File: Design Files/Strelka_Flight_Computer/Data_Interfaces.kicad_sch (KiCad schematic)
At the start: 10 parts

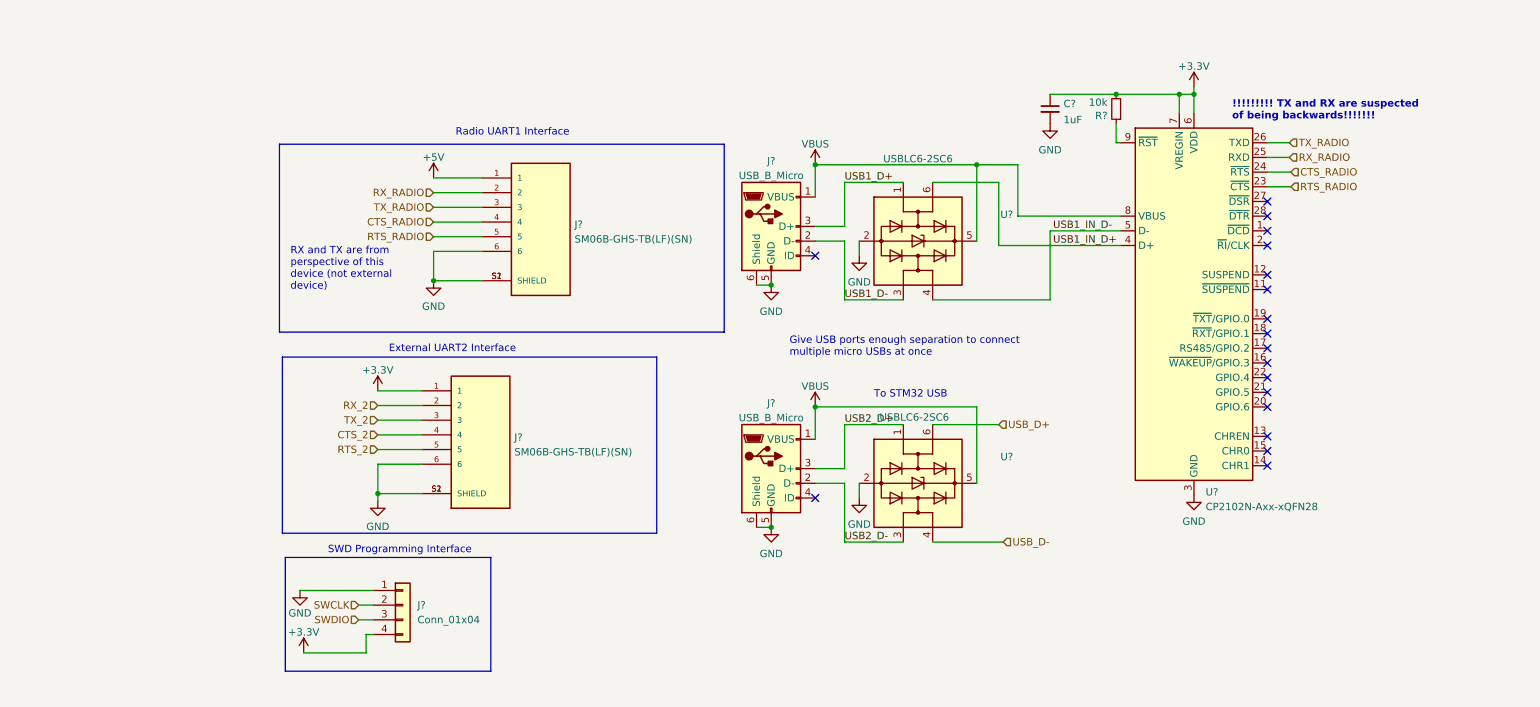
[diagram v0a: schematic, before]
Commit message: Added sensors
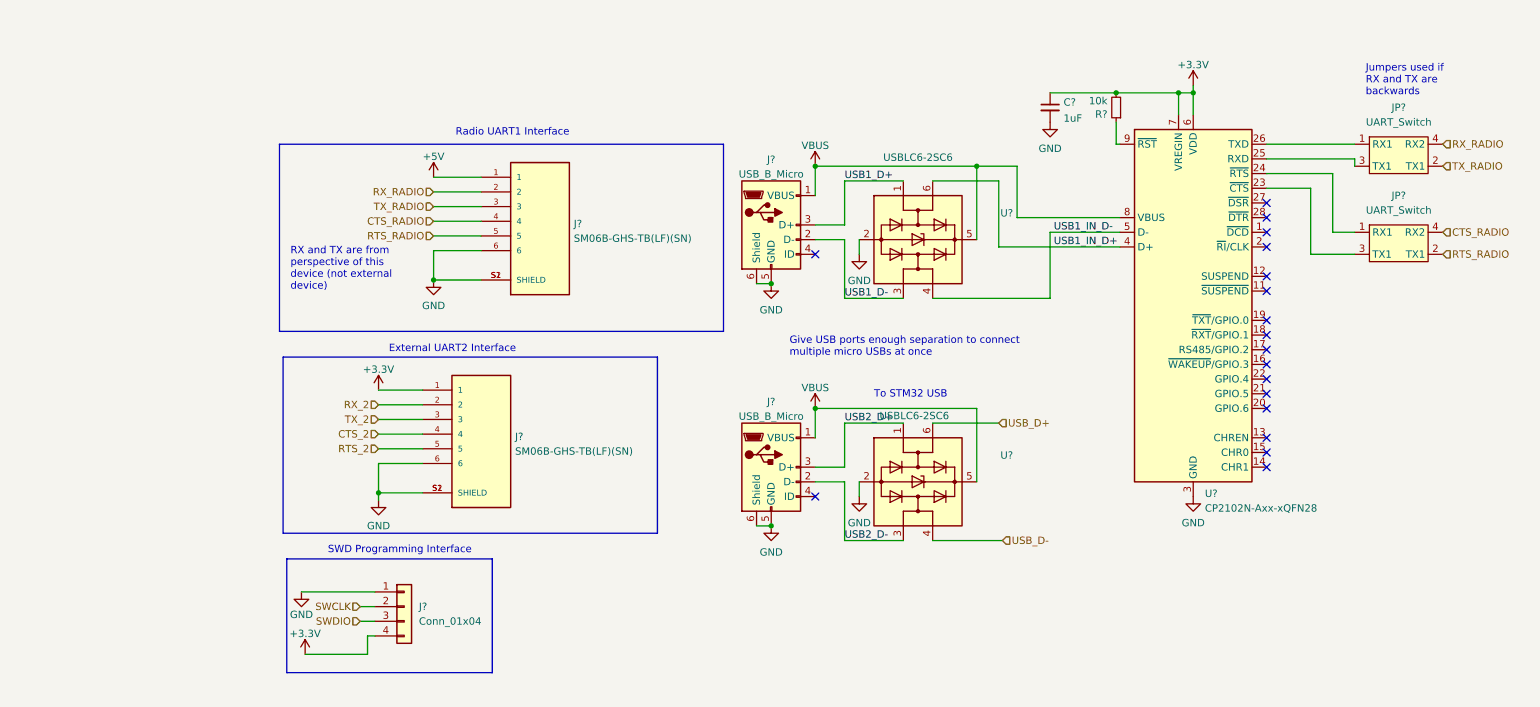
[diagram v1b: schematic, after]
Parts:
- added JP? (x2): UART_Switch, Footprints:UART_Switch, symbol UART_Switch:UART_Switch
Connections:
- net CTS_RADIO: now also JP?.4 (RX2); no longer U?.24 (~{RTS})
- net RTS_RADIO: now also JP?.2 (TX1); no longer U?.23 (~{CTS})
- net RX_RADIO: now also JP?.4 (RX2); no longer U?.25 (RXD)
- net TX_RADIO: now also JP?.2 (TX1); no longer U?.26 (TXD)
- new net: JP?.1 (RX1), U?.24 (~{RTS})
- new net: JP?.3 (TX1), U?.23 (~{CTS})
- new net: JP?.1 (RX1), U?.26 (TXD)
- new net: JP?.3 (TX1), U?.25 (RXD)
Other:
- note added: "Jumpers used if RX and TX are backwards"
- note removed: "!!!!!!!!! TX and RX are suspected of being backwards!!!!!!!"

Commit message: Working SPICE sim for ematch continuity circuit
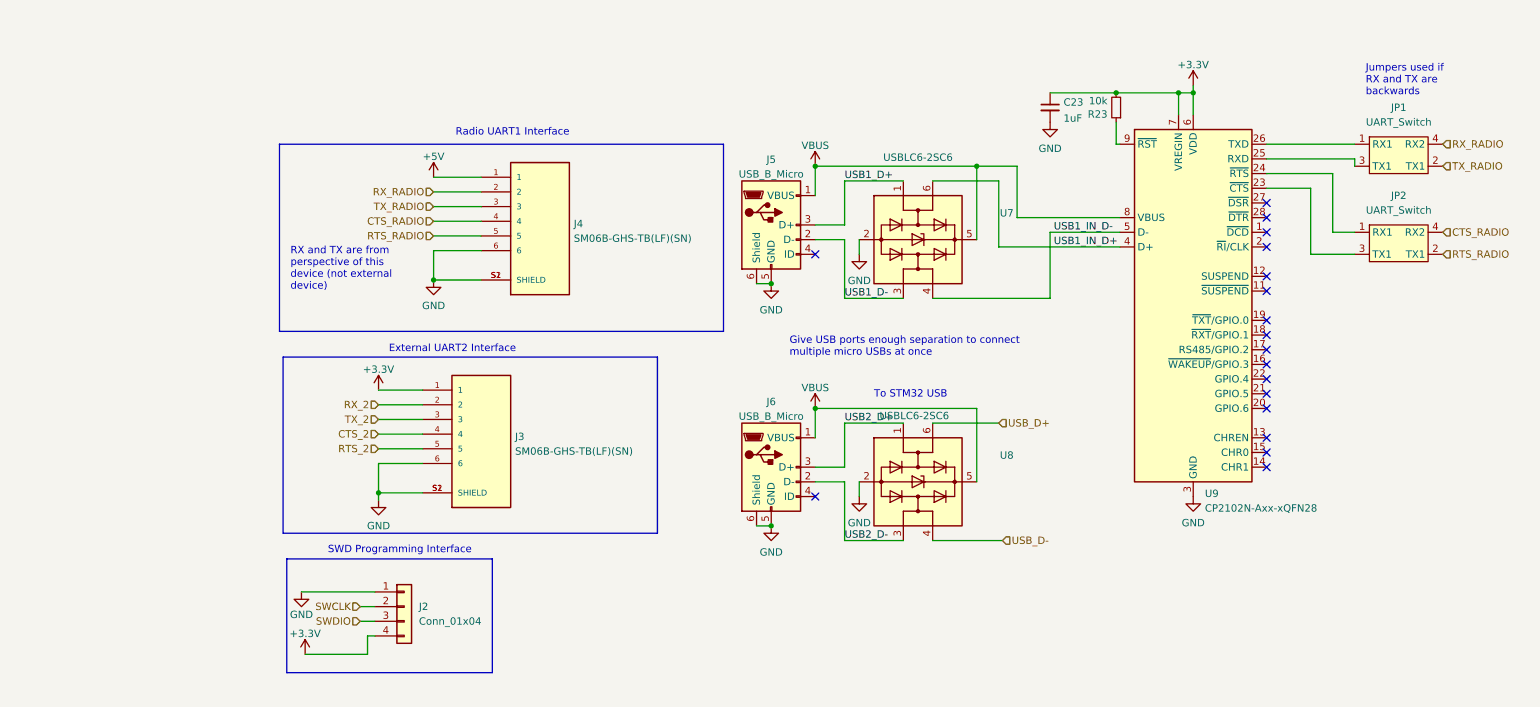
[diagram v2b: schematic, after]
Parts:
- gave numbers to parts that had none: 12
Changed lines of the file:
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@@
   (symbol (lib_id "power:GND") (at 84.455 100.965 0) (unit 1)
     (in_bom yes) (on_board yes) (fields_autoplaced)
-    (property "Reference" "#PWR?" (id 0) (at 84.455 107.315 0)
+    (property "Reference" "#PWR0158" (id 0) (at 84.455 107.315 0)
       (effects (font (size 1.27 1.27)) hide)
     )
@@
   (symbol (lib_id "power:VBUS") (at 160.02 43.18 0) (unit 1)
     (in_bom yes) (on_board yes) (fields_autoplaced)
-    (property "Reference" "#PWR?" (id 0) (at 160.02 46.99 0)
+    (property "Reference" "#PWR0155" (id 0) (at 160.02 46.99 0)
       (effects (font (size 1.27 1.27)) hide)
     )
@@
   (symbol (lib_id "Device:C_Small") (at 200.66 33.02 0) (unit 1)
     (in_bom yes) (on_board yes)
-    (property "Reference" "C?" (id 0) (at 202.9842 32.1115 0)
+    (property "Reference" "C23" (id 0) (at 202.9842 32.1115 0)
       (effects (font (size 1.27 1.27)) (justify left))
     )
@@
   (symbol (lib_id "Power_Protection:USBLC6-2SC6") (at 177.8 55.88 270) (unit 1)
     (in_bom yes) (on_board yes)
-    (property "Reference" "U?" (id 0) (at 193.1557 51.2911 90))
+    (property "Reference" "U7" (id 0) (at 193.1557 51.2911 90))
     (property "Value" "USBLC6-2SC6" (id 1) (at 177.8 41.656 90))
     (property "Footprint" "Package_TO_SOT_SMD:SOT-23-6" (id 2) (at 165.1 55.88 0)
@@
   (symbol (lib_id "power:GND") (at 71.12 116.84 0) (unit 1)
     (in_bom yes) (on_board yes)
-    (property "Reference" "#PWR?" (id 0) (at 71.12 123.19 0)
+    (property "Reference" "#PWR0156" (id 0) (at 71.12 123.19 0)
       (effects (font (size 1.27 1.27)) hide)
     )
@@
   (symbol (lib_id "power:GND") (at 167.64 100.33 0) (unit 1)
     (in_bom yes) (on_board yes) (fields_autoplaced)
-    (property "Reference" "#PWR?" (id 0) (at 167.64 106.68 0)
+    (property "Reference" "#PWR0149" (id 0) (at 167.64 106.68 0)
       (effects (font (size 1.27 1.27)) hide)
     )
@@
   (symbol (lib_id "Nebula-rescue:R_Small-Device-H7_FlightComputer-rescue") (at 212.09 33.02 180) (unit 1)
     (in_bom yes) (on_board yes)
-    (property "Reference" "R?" (id 0) (at 210.5914 34.1884 0)
+    (property "Reference" "R23" (id 0) (at 210.5914 34.1884 0)
       (effects (font (size 1.27 1.27)) (justify left))
     )
@@
   (symbol (lib_id "Power_Protection:USBLC6-2SC6") (at 177.8 97.79 270) (unit 1)
     (in_bom yes) (on_board yes)
-    (property "Reference" "U?" (id 0) (at 193.1557 93.2011 90))
+    (property "Reference" "U8" (id 0) (at 193.1557 93.2011 90))
     (property "Value" "USBLC6-2SC6" (id 1) (at 177.165 86.36 90))
     (property "Footprint" "Package_TO_SOT_SMD:SOT-23-6" (id 2) (at 165.1 97.79 0)
@@
   (symbol (lib_id "power:+5V") (at 93.98 45.085 0) (unit 1)
     (in_bom yes) (on_board yes) (fields_autoplaced)
-    (property "Reference" "#PWR?" (id 0) (at 93.98 48.895 0)
+    (property "Reference" "#PWR0160" (id 0) (at 93.98 48.895 0)
       (effects (font (size 1.27 1.27)) hide)
     )
@@
   (symbol (lib_id "power:GND") (at 200.66 35.56 0) (unit 1)
     (in_bom yes) (on_board yes) (fields_autoplaced)
-    (property "Reference" "#PWR?" (id 0) (at 200.66 41.91 0)
+    (property "Reference" "#PWR0154" (id 0) (at 200.66 41.91 0)
       (effects (font (size 1.27 1.27)) hide)
     )
@@
   (symbol (lib_id "Connector:USB_B_Micro") (at 152.4 53.34 0) (unit 1)
     (in_bom yes) (on_board yes) (fields_autoplaced)
-    (property "Reference" "J?" (id 0) (at 152.4 42.0202 0))
+    (property "Reference" "J5" (id 0) (at 152.4 42.0202 0))
     (property "Value" "USB_B_Micro" (id 1) (at 152.4 44.5571 0))
     (property "Footprint" "Connector_USB:USB_Micro-B_Molex-105017-0001" (id 2) (at 156.21 54.61 0)
@@
   (symbol (lib_id "Connector_Generic:Conn_01x04") (at 88.9 119.38 0) (unit 1)
     (in_bom yes) (on_board yes) (fields_autoplaced)
-    (property "Reference" "J?" (id 0) (at 91.44 119.3799 0)
+    (property "Reference" "J2" (id 0) (at 91.44 119.3799 0)
       (effects (font (size 1.27 1.27)) (justify left))
     )
@@
   (symbol (lib_id "SM06B-GHS-TB_LF__SN_:SM06B-GHS-TB(LF)(SN)") (at 112.395 52.705 0) (unit 1)
     (in_bom yes) (on_board yes) (fields_autoplaced)
-    (property "Reference" "J?" (id 0) (at 118.237 53.1403 0)
+    (property "Reference" "J4" (id 0) (at 118.237 53.1403 0)
       (effects (font (size 1.27 1.27)) (justify left))
     )
@@
   (symbol (lib_id "UART_Switch:UART_Switch") (at 260.985 57.15 0) (unit 1)
     (in_bom yes) (on_board yes) (fields_autoplaced)
-    (property "Reference" "JP?" (id 0) (at 260.985 48.26 0))
+    (property "Reference" "JP2" (id 0) (at 260.985 48.26 0))
     (property "Value" "UART_Switch" (id 1) (at 260.985 50.8 0))
     (property "Footprint" "Footprints:UART_Switch" (id 2) (at 260.985 57.15 0)
@@
   (symbol (lib_id "power:VBUS") (at 160.02 85.09 0) (unit 1)
     (in_bom yes) (on_board yes) (fields_autoplaced)
-    (property "Reference" "#PWR?" (id 0) (at 160.02 88.9 0)
+    (property "Reference" "#PWR0151" (id 0) (at 160.02 88.9 0)
       (effects (font (size 1.27 1.27)) hide)
     )
@@
   (symbol (lib_id "Connector:USB_B_Micro") (at 152.4 95.25 0) (unit 1)
     (in_bom yes) (on_board yes) (fields_autoplaced)
-    (property "Reference" "J?" (id 0) (at 152.4 83.9302 0))
+    (property "Reference" "J6" (id 0) (at 152.4 83.9302 0))
     (property "Value" "USB_B_Micro" (id 1) (at 152.4 86.4671 0))
     (property "Footprint" "Connector_USB:USB_Micro-B_Molex-105017-0001" (id 2) (at 156.21 96.52 0)
@@
   (symbol (lib_id "power:GND") (at 152.4 105.41 0) (unit 1)
     (in_bom yes) (on_board yes) (fields_autoplaced)
-    (property "Reference" "#PWR?" (id 0) (at 152.4 111.76 0)
+    (property "Reference" "#PWR0150" (id 0) (at 152.4 111.76 0)
       (effects (font (size 1.27 1.27)) hide)
     )
@@
   (symbol (lib_id "SM06B-GHS-TB_LF__SN_:SM06B-GHS-TB(LF)(SN)") (at 102.235 89.535 0) (unit 1)
     (in_bom yes) (on_board yes) (fields_autoplaced)
-    (property "Reference" "J?" (id 0) (at 108.077 89.9703 0)
+    (property "Reference" "J3" (id 0) (at 108.077 89.9703 0)
       (effects (font (size 1.27 1.27)) (justify left))
     )
@@
   (symbol (lib_id "power:+3.3V") (at 84.455 81.915 0) (unit 1)
     (in_bom yes) (on_board yes) (fields_autoplaced)
-    (property "Reference" "#PWR?" (id 0) (at 84.455 85.725 0)
+    (property "Reference" "#PWR0159" (id 0) (at 84.455 85.725 0)
       (effects (font (size 1.27 1.27)) hide)
     )
@@
   (symbol (lib_id "power:GND") (at 225.425 100.33 0) (unit 1)
     (in_bom yes) (on_board yes) (fields_autoplaced)
-    (property "Reference" "#PWR?" (id 0) (at 225.425 106.68 0)
+    (property "Reference" "#PWR0148" (id 0) (at 225.425 106.68 0)
       (effects (font (size 1.27 1.27)) hide)
     )
@@
   (symbol (lib_id "UART_Switch:UART_Switch") (at 260.985 41.91 0) (unit 1)
     (in_bom yes) (on_board yes) (fields_autoplaced)
-    (property "Reference" "JP?" (id 0) (at 260.985 33.02 0))
+    (property "Reference" "JP1" (id 0) (at 260.985 33.02 0))
     (property "Value" "UART_Switch" (id 1) (at 260.985 35.56 0))
     (property "Footprint" "Footprints:UART_Switch" (id 2) (at 260.985 41.91 0)
@@
   (symbol (lib_id "power:GND") (at 93.98 62.865 0) (unit 1)
     (in_bom yes) (on_board yes) (fields_autoplaced)
-    (property "Reference" "#PWR?" (id 0) (at 93.98 69.215 0)
+    (property "Reference" "#PWR0161" (id 0) (at 93.98 69.215 0)
       (effects (font (size 1.27 1.27)) hide)
     )
@@
   (symbol (lib_id "power:+3.3V") (at 71.755 127.635 0) (unit 1)
     (in_bom yes) (on_board yes) (fields_autoplaced)
-    (property "Reference" "#PWR?" (id 0) (at 71.755 131.445 0)
+    (property "Reference" "#PWR0157" (id 0) (at 71.755 131.445 0)
       (effects (font (size 1.27 1.27)) hide)
     )
@@
   (symbol (lib_id "power:GND") (at 167.64 58.42 0) (unit 1)
     (in_bom yes) (on_board yes) (fields_autoplaced)
-    (property "Reference" "#PWR?" (id 0) (at 167.64 64.77 0)
+    (property "Reference" "#PWR0152" (id 0) (at 167.64 64.77 0)
       (effects (font (size 1.27 1.27)) hide)
     )
@@
   (symbol (lib_id "power:GND") (at 152.4 63.5 0) (unit 1)
     (in_bom yes) (on_board yes) (fields_autoplaced)
-    (property "Reference" "#PWR?" (id 0) (at 152.4 69.85 0)
+    (property "Reference" "#PWR0153" (id 0) (at 152.4 69.85 0)
       (effects (font (size 1.27 1.27)) hide)
     )
@@
   (symbol (lib_id "Interface_USB:CP2102N-Axx-xQFN28") (at 225.425 67.31 0) (unit 1)
     (in_bom yes) (on_board yes) (fields_autoplaced)
-    (property "Reference" "U?" (id 0) (at 227.4444 99.8204 0)
+    (property "Reference" "U9" (id 0) (at 227.4444 99.8204 0)
       (effects (font (size 1.27 1.27)) (justify left))
     )
@@
   (symbol (lib_id "power:+3.3V") (at 225.425 29.21 0) (unit 1)
     (in_bom yes) (on_board yes) (fields_autoplaced)
-    (property "Reference" "#PWR?" (id 0) (at 225.425 33.02 0)
-      (effects (font (size 1.27 1.27)) hide)
-    )
+    (property "Reference" "#PWR0147" (id 0) (at 225.425 33.02 0)
+      (effects (font (size 1.27 1.27)) hide)
+    )

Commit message: Added power board, almost finished Strelka schematic
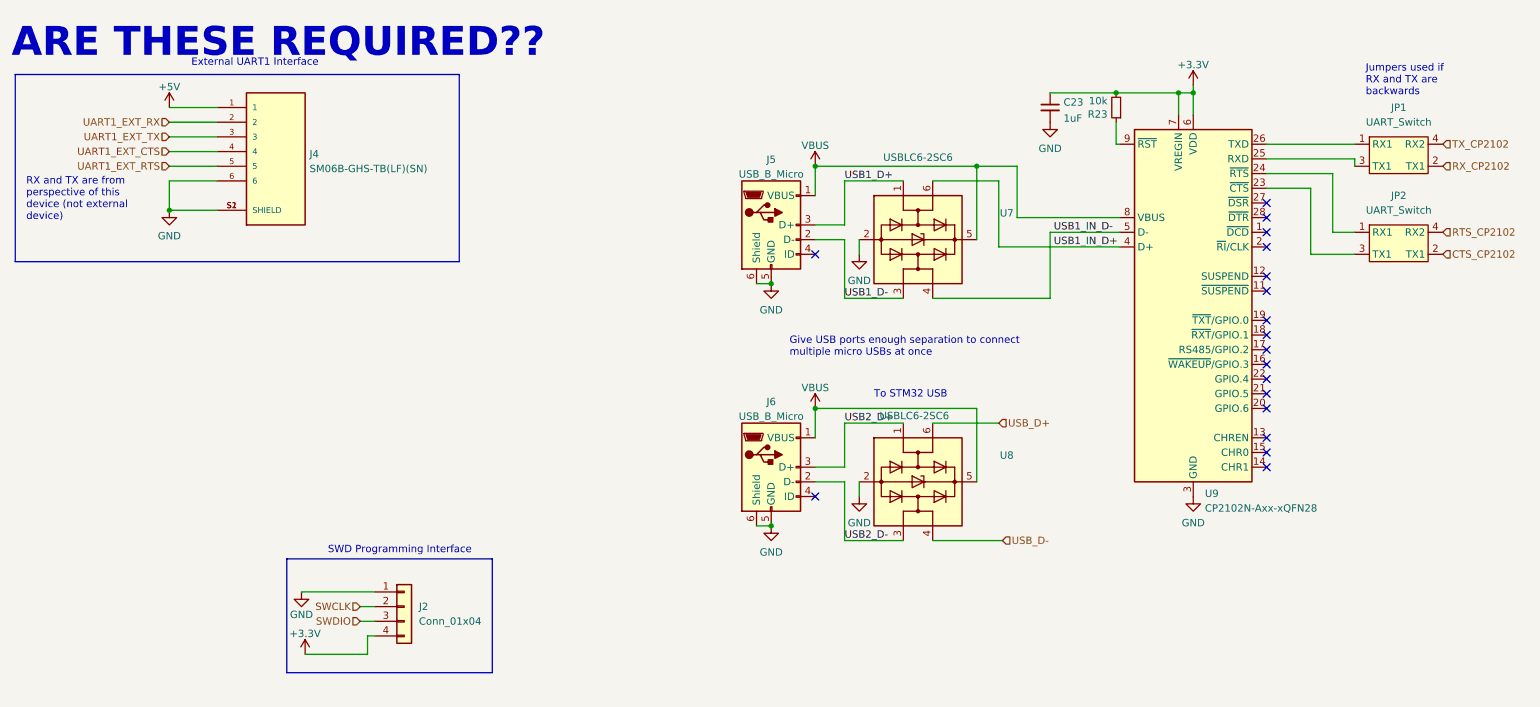
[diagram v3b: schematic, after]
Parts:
- removed J3: SM06B-GHS-TB(LF)(SN), Footprints:JST_SM06B-GHS-TB(LF)(SN), symbol SM06B-GHS-TB_LF__SN_:SM06B-GHS-TB(LF)(SN)
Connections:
- net CTS_RADIO renamed RTS_CP2102
- net RTS_CP2102: no longer J4.4
- net RTS_RADIO renamed CTS_CP2102
- net CTS_CP2102: no longer J4.5
- net RX_RADIO renamed TX_CP2102
- net TX_CP2102: no longer J4.2
- net TX_RADIO renamed RX_CP2102
- net RX_CP2102: no longer J4.3
- new net UART1_EXT_CTS: J4.4
- new net UART1_EXT_RTS: J4.5
- new net UART1_EXT_RX: J4.2
- new net UART1_EXT_TX: J4.3
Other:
- note added: "ARE THESE REQUIRED??"
- note added: "External UART1 Interface"
- note removed: "External UART2 Interface"
- note removed: "Radio UART1 Interface"
- moved on the sheet: J4

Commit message: Pin mapping and created STM32 .ioc for reference
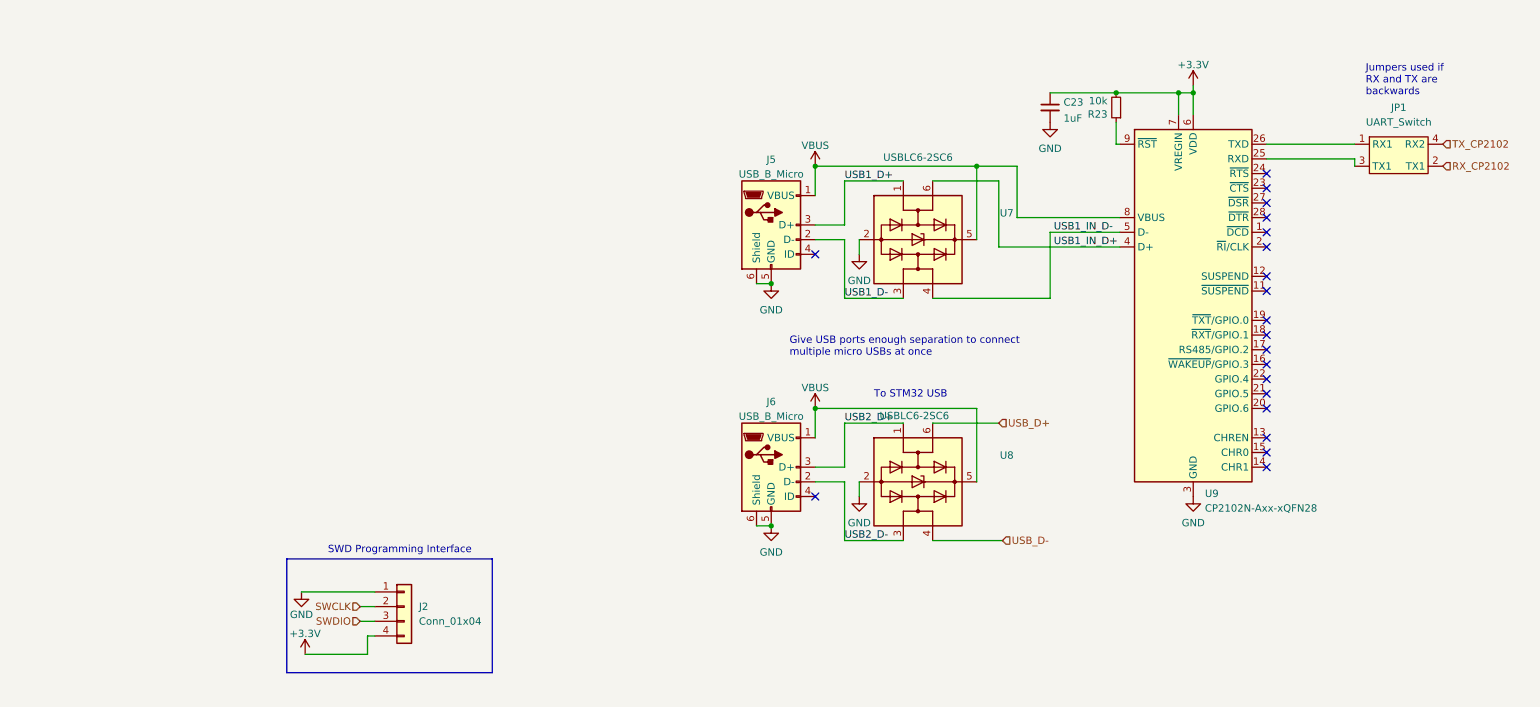
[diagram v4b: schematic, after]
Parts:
- removed J4: SM06B-GHS-TB(LF)(SN), Footprints:JST_SM06B-GHS-TB(LF)(SN), symbol SM06B-GHS-TB_LF__SN_:SM06B-GHS-TB(LF)(SN)
- removed JP2: UART_Switch, Footprints:UART_Switch, symbol UART_Switch:UART_Switch
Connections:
- no-connect marks 18 -> 20
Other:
- note removed: "ARE THESE REQUIRED??"
- note removed: "External UART1 Interface"
- note removed: "RX and TX are from perspective of this device (not external device)"
